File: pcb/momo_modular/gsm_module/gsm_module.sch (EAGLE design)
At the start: 20 parts, among them U1 PIC16LF1823, U2 TI-HIGHSIDE-PFET, U3 SIM900

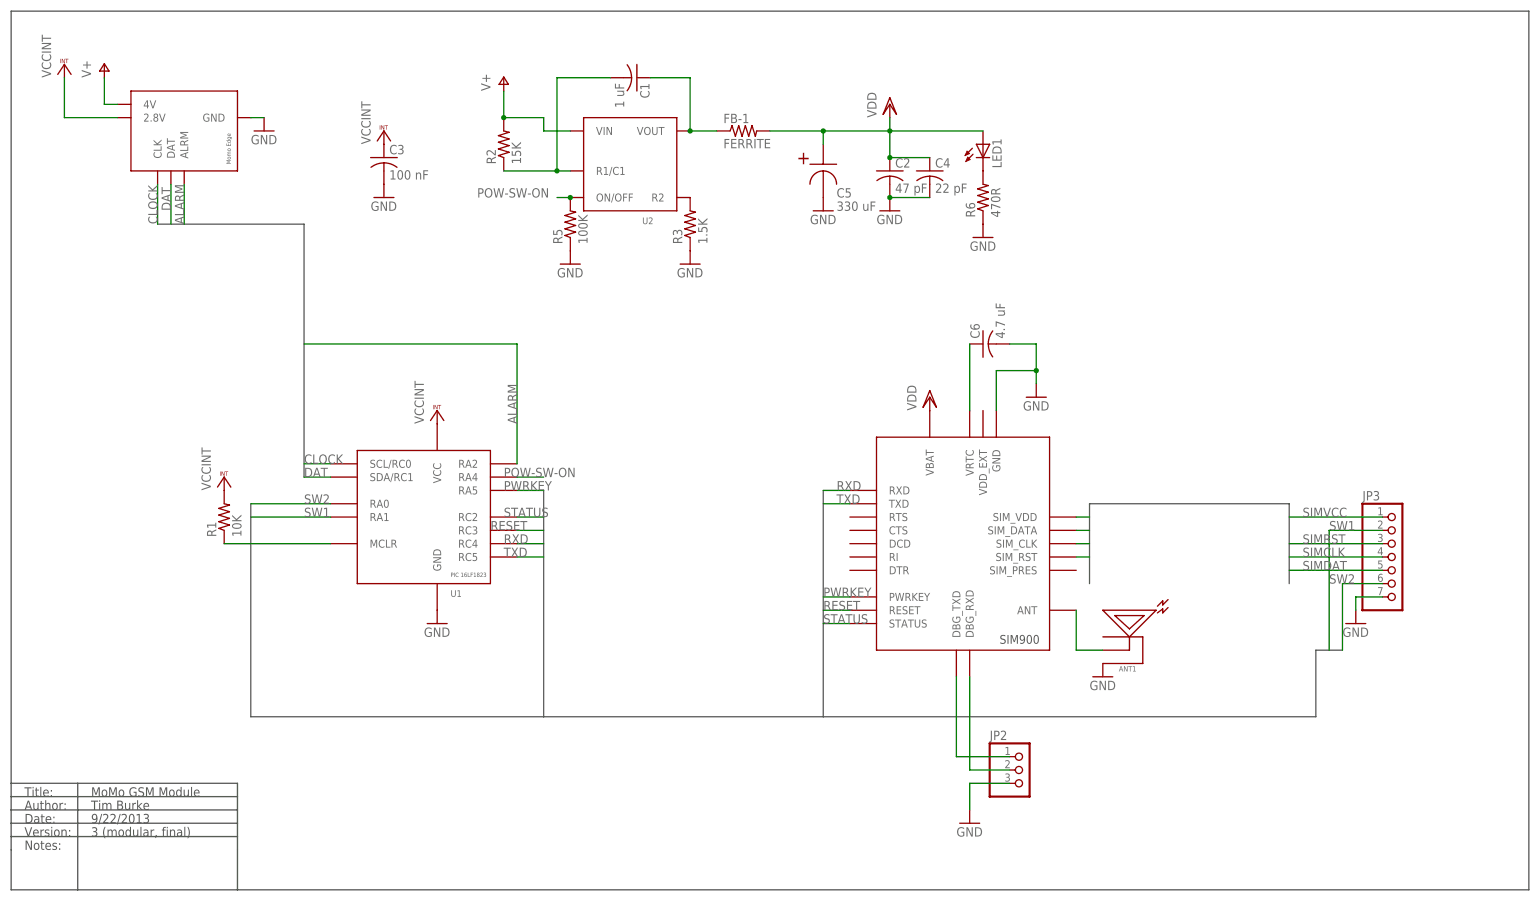
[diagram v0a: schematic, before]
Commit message: Make GSM board fit into 1.3x2" board.
- Removes need for separate Card Adapter board
- GSM module now has integrated SIM Card holder
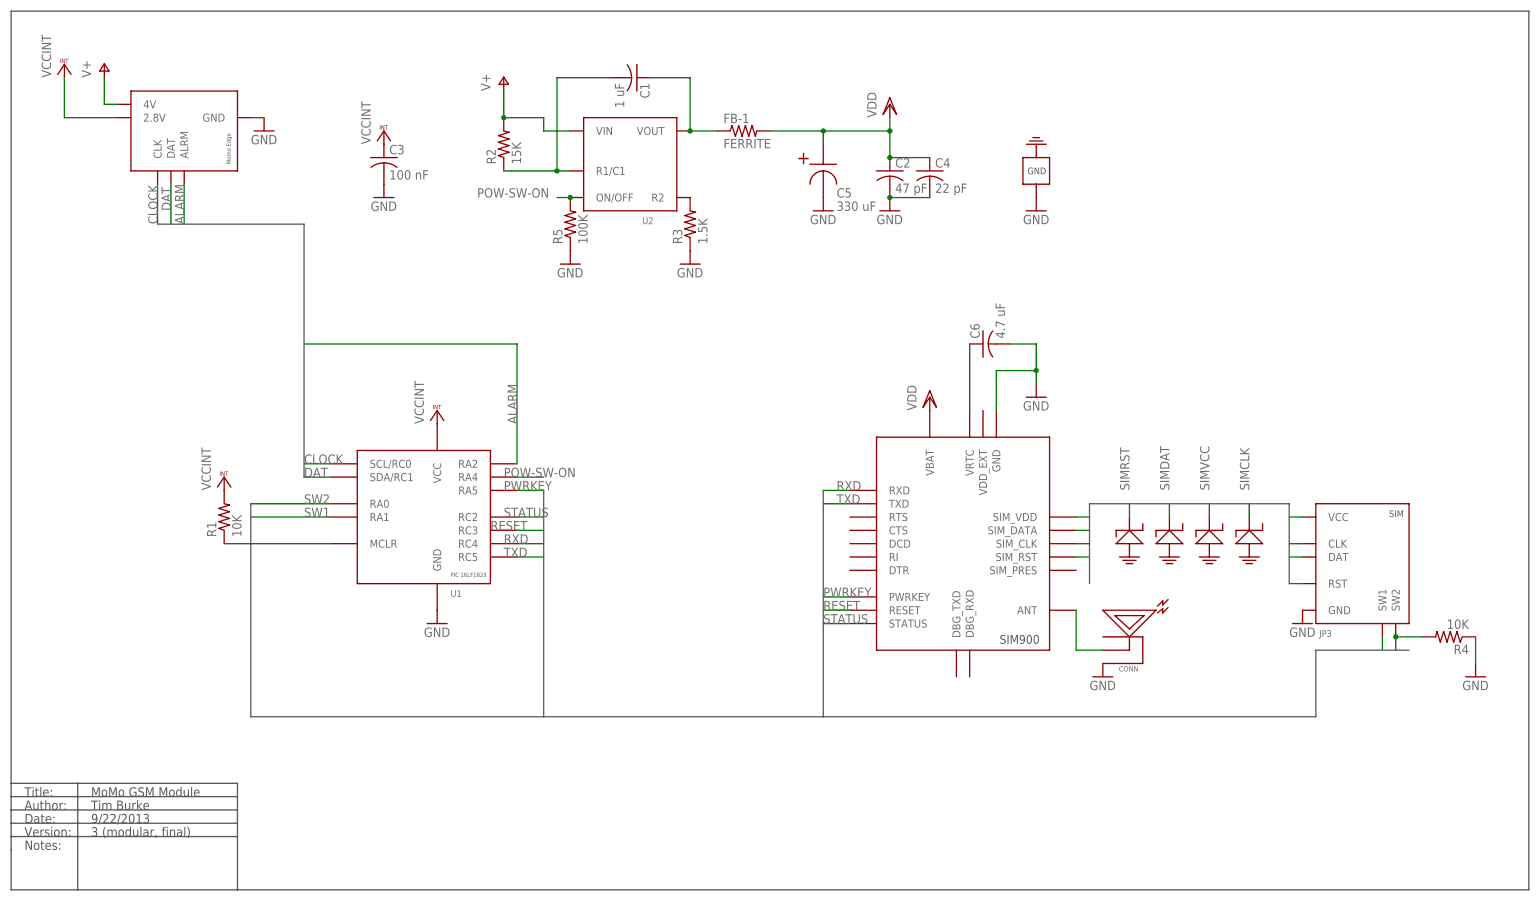
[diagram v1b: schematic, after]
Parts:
- removed JP2: (no value), pinhead:PINHD-1X3
- removed LED1: (no value), led:LEDCHIPLED_0603
- removed R6: 470R, rcl:R-US_R0603
- added R4: 10K, rcl:R-US_R0603
- added U4: ESD-SMF05C, components:ESD-SMF05C
- CONN: DESCRIPTION RF antenna connector u.fl -> (none); FOOTPRINT Custom SMD -> (none)
- FB-1: DESCRIPTION Ferrite Bead -> (none); FOOTPRINT SMD 0805 -> (none)
- JP3: value (none) -> SIMHOLDER-8PINHING; device pinhead:PINHD-1X7 -> components:SIMHOLDER-8PINHING; DESCRIPTION 7 pin vertical male header -> (none); FOOTPRINT Through Hole -> (none)
- renumbered ANT1 to CONN
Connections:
- removed net DEBUGRX: JP2.2, U3.DBG_RXD
- removed net DEBUGTX: JP2.1, U3.DBG_TXD
- removed net N$2: LED1.C, R6.2
- net GND: now also JP3.GND, R4.1, U4G$6.GND; no longer JP2.3, JP3.7, R6.1
- net SIMCLK: now also JP3.CLK, U4G$2.P$1; no longer JP3.4
- net SIMDAT: now also JP3.DAT, U4G$4.P$1; no longer JP3.5
- net SIMRST: now also JP3.RST, U4G$1.P$1; no longer JP3.3
- net SIMVCC: now also JP3.VCC, U4G$3.P$1; no longer JP3.1
- net SW1: now also JP3.SW1; no longer JP3.2
- net SW2: now also JP3.SW2, R4.2; no longer JP3.6
- net VDD: no longer LED1.A

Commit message: Fix gsm layout based on measured SIM900 module size.
U1 and C5 would be very close to the module so I relaid it out in
order to maximize the distance between the SIM900 and those two
components.  Also, C5 was swapped for a smaller tantalum capacitor
since the ripple current was calculated too conservatively last time.
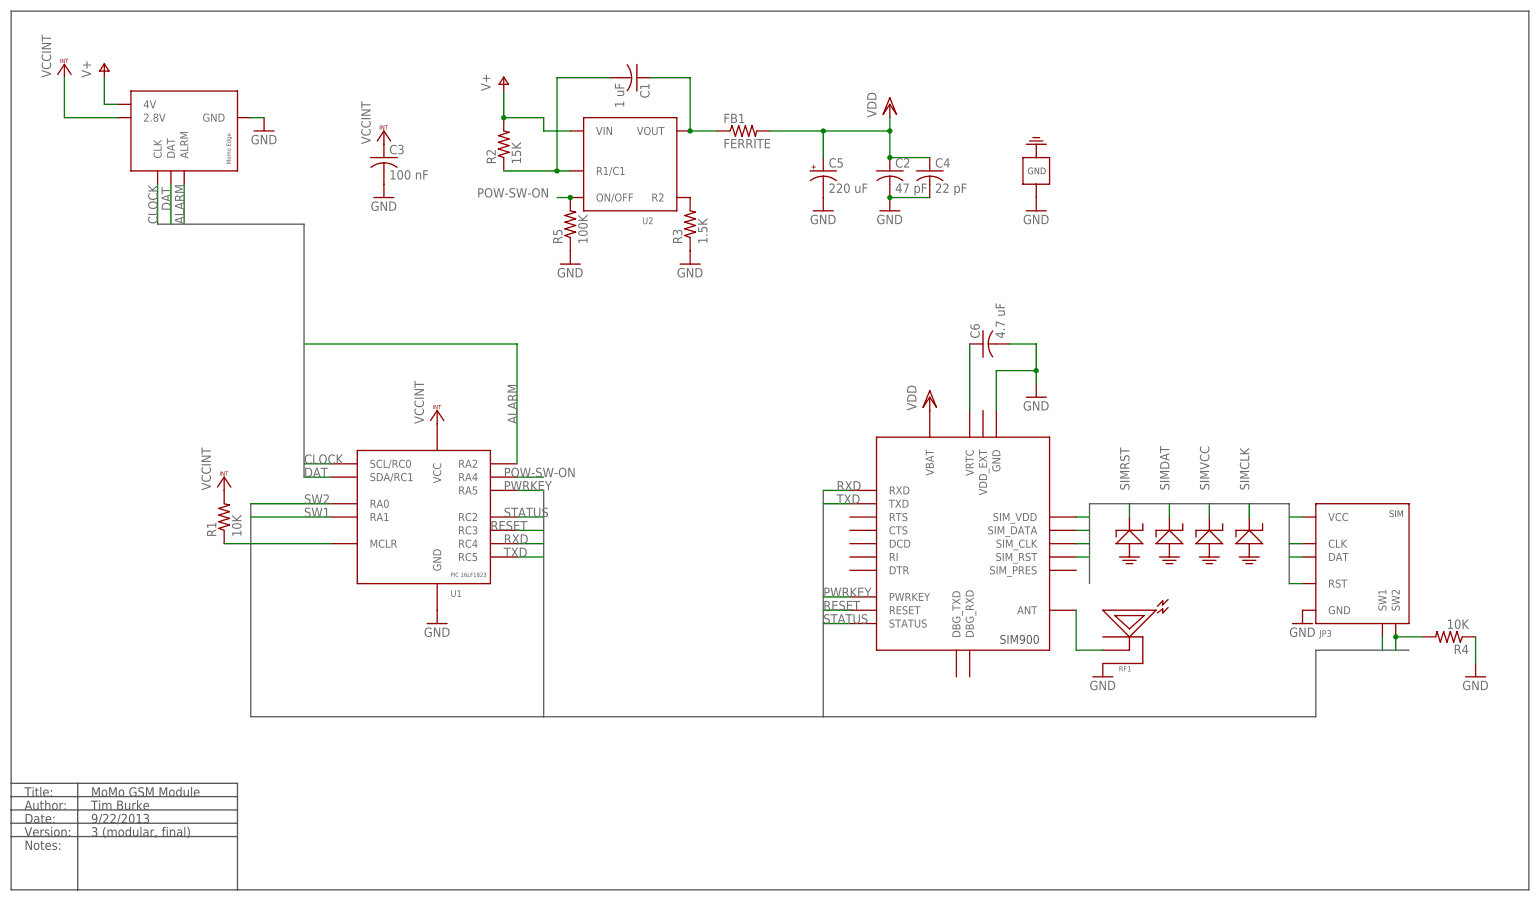
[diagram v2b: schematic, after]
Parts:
- C5: value 330 uF -> 220 uF; device components:TANTALUM_CAP -> rcl:CPOL-USCT3528
- renumbered CONN to RF1, FB-1 to FB1
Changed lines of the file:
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@@
 <?xml version="1.0" encoding="utf-8"?>
 <!DOCTYPE eagle SYSTEM "eagle.dtd">
-<eagle version="6.4">
+<eagle version="6.5.0">
 <drawing>
 <settings>
@@
 </part>
 <part name="GND3" library="supply1" deviceset="GND" device=""/>
-<part name="FB-1" library="rcl" deviceset="R-US_" device="R0805" value="FERRITE">
+<part name="FB1" library="rcl" deviceset="R-US_" device="R0805" value="FERRITE">
 <attribute name="DIGIKEY-PN" value="445-1567-1-ND"/>
 </part>
@@
 <part name="GND11" library="supply1" deviceset="GND" device=""/>
 <part name="GND12" library="supply1" deviceset="GND" device=""/>
-<part name="CONN" library="components" deviceset="RFANTENNA" device="">
+<part name="RF1" library="components" deviceset="RFANTENNA" device="">
 <attribute name="DIGIKEY-PN" value="J983CT-ND"/>
 </part>
@@
 <part name="U2" library="components" deviceset="TI-HIGHSIDE-PFET" device=""/>
 <part name="U3" library="components" deviceset="SIM900" device=""/>
-<part name="C5" library="components" deviceset="TANTALUM_CAP" device="" value="330 uF"/>
 <part name="JP3" library="components" deviceset="SIMHOLDER-8PIN" device="HING"/>
 <part name="GND8" library="supply1" deviceset="GND" device=""/>
@@
 <attribute name="DIGIKEY-PN" value="1276-1259-1-ND"/>
 </part>
+<part name="C5" library="rcl" deviceset="CPOL-US" device="CT3528" value="220 uF"/>
 </parts>
 <sheets>
@@
 <wire x1="20.32" y1="-38.1" x2="20.32" y2="-40.64" width="0.254" layer="97"/>
 <wire x1="20.32" y1="-40.64" x2="20.32" y2="-43.18" width="0.254" layer="97"/>
-<wire x1="20.32" y1="-43.18" x2="20.32" y2="-45.72" width="0.254" layer="97"/>
-<wire x1="20.32" y1="-45.72" x2="20.32" y2="-53.34" width="0.254" layer="97"/>
+<wire x1="20.32" y1="-43.18" x2="20.32" y2="-53.34" width="0.254" layer="97"/>
 <wire x1="20.32" y1="-53.34" x2="-10.16" y2="-53.34" width="0.254" layer="97"/>
 <wire x1="-10.16" y1="-53.34" x2="-22.86" y2="-53.34" width="0.254" layer="97"/>
-<wire x1="-22.86" y1="-53.34" x2="-22.86" y2="-45.72" width="0.254" layer="97"/>
-<wire x1="-22.86" y1="-45.72" x2="-22.86" y2="-43.18" width="0.254" layer="97"/>
+<wire x1="-22.86" y1="-53.34" x2="-22.86" y2="-43.18" width="0.254" layer="97"/>
 <wire x1="-22.86" y1="-43.18" x2="-22.86" y2="-40.64" width="0.254" layer="97"/>
 <wire x1="-22.86" y1="-40.64" x2="-22.86" y2="-38.1" width="0.254" layer="97"/>
@@
 </instance>
 <instance part="GND3" gate="1" x="106.68" y="66.04"/>
-<instance part="FB-1" gate="G$1" x="116.84" y="91.44">
+<instance part="FB1" gate="G$1" x="116.84" y="91.44">
 <attribute name="DIGIKEY-PN" x="116.84" y="91.44" size="1.778" layer="96" display="off"/>
 </instance>
@@
 <instance part="GND11" gate="1" x="223.52" y="-2.54"/>
 <instance part="GND12" gate="1" x="172.72" y="76.2"/>
-<instance part="CONN" gate="G$1" x="185.42" y="-10.16">
+<instance part="RF1" gate="G$1" x="185.42" y="-10.16">
 <attribute name="DIGIKEY-PN" x="185.42" y="-10.16" size="1.778" layer="96" display="off"/>
 </instance>
@@
 <instance part="U2" gate="G$1" x="93.98" y="81.28"/>
 <instance part="U3" gate="G$1" x="152.4" y="15.24"/>
-<instance part="C5" gate="G$1" x="132.08" y="81.28"/>
 <instance part="JP3" gate="G$1" x="226.06" y="5.08"/>
 <instance part="GND8" gate="1" x="256.54" y="-12.7"/>
@@
 <attribute name="DIGIKEY-PN" x="162.56" y="50.8" size="1.778" layer="96" rot="R90" display="off"/>
 </instance>
+<instance part="C5" gate="G$1" x="132.08" y="83.82"/>
 </instances>
 <busses>
@@
 </segment>
 <segment>
-<pinref part="CONN" gate="G$1" pin="SHIELD"/>
+<pinref part="RF1" gate="G$1" pin="SHIELD"/>
 <pinref part="GND13" gate="1" pin="GND"/>
 </segment>
@@
 <wire x1="99.06" y1="101.6" x2="106.68" y2="101.6" width="0.1524" layer="91"/>
 <wire x1="106.68" y1="101.6" x2="106.68" y2="91.44" width="0.1524" layer="91"/>
-<pinref part="FB-1" gate="G$1" pin="1"/>
+<pinref part="FB1" gate="G$1" pin="1"/>
 <wire x1="106.68" y1="91.44" x2="111.76" y2="91.44" width="0.1524" layer="91"/>
 <pinref part="U2" gate="G$1" pin="VOUT"/>
@@
 <net name="VDD" class="0">
 <segment>
-<pinref part="FB-1" gate="G$1" pin="2"/>
+<pinref part="FB1" gate="G$1" pin="2"/>
 <pinref part="VDD1" gate="G$1" pin="VDD"/>
 <wire x1="121.92" y1="91.44" x2="132.08" y2="91.44" width="0.1524" layer="91"/>
@@
 <junction x="144.78" y="86.36"/>
 <junction x="144.78" y="91.44"/>
+<junction x="132.08" y="91.44"/>
 <pinref part="C5" gate="G$1" pin="+"/>
-<wire x1="132.08" y1="88.9" x2="132.08" y2="91.44" width="0.1524" layer="91"/>
-<junction x="132.08" y="91.44"/>
+<wire x1="132.08" y1="86.36" x2="132.08" y2="91.44" width="0.1524" layer="91"/>
 </segment>
 <segment>
@@
 <segment>
 <wire x1="180.34" y1="0" x2="180.34" y2="-7.62" width="0.1524" layer="91"/>
-<pinref part="CONN" gate="G$1" pin="PIN"/>
+<pinref part="RF1" gate="G$1" pin="PIN"/>
 <wire x1="180.34" y1="-7.62" x2="185.42" y2="-7.62" width="0.1524" layer="91"/>
 <pinref part="U3" gate="G$1" pin="ANT"/>

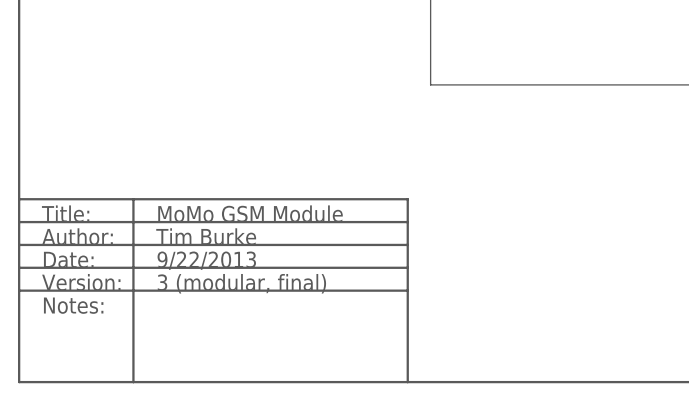
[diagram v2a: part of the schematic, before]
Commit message: Fix gsm module to not have sim card adapter hang over board edge
- This would have meant that the board could not be routed post
smt assembly and that the board could not have been panelized at
2x1.3" since the part would not have been assemblable.
- As a consequence, I had to get rid of the screw holes for this
module.
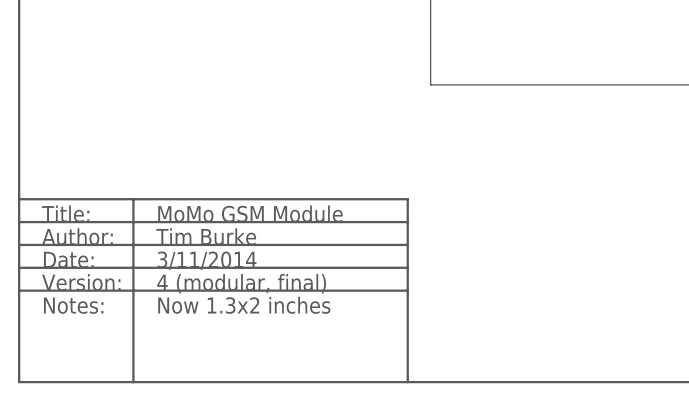
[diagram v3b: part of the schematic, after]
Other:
- note added: "3/11/2014"
- note added: "4 (modular, final)"
- note added: "Now 1.3x2 inches"
- note removed: "3 (modular, final)"
- note removed: "9/22/2013"
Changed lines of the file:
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@@
 <text x="-7.62" y="-35.56" size="1.778" layer="97">MoMo GSM Module</text>
 <text x="-7.62" y="-38.1" size="1.778" layer="97">Tim Burke</text>
-<text x="-7.62" y="-40.64" size="1.778" layer="97">9/22/2013</text>
-<text x="-7.62" y="-43.18" size="1.778" layer="97">3 (modular, final)</text>
+<text x="-7.62" y="-40.64" size="1.778" layer="97">3/11/2014</text>
+<text x="-7.62" y="-43.18" size="1.778" layer="97">4 (modular, final)</text>
+<text x="-7.62" y="-45.72" size="1.778" layer="97">Now 1.3x2 inches</text>
 </plain>
 <instances>
